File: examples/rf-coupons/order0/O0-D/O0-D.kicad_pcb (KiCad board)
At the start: 4 copper layers, 90.6 x 51.5 mm, 29 parts, among them X20 Anchor, X23 Anchor, X26 Anchor

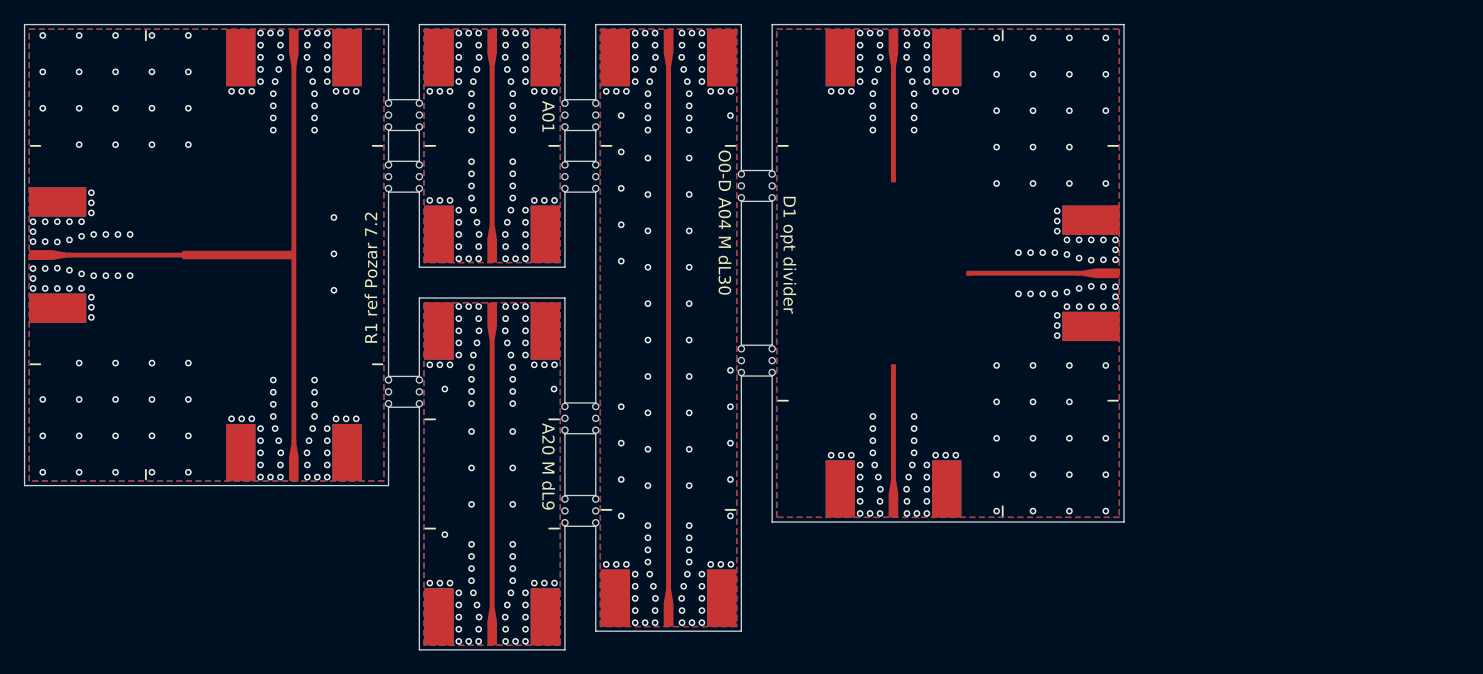
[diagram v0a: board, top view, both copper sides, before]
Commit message: Order 0: D1 re-optimized under the corner-gap DRC (d1-star 7e070ca8), O0-D regenerated, pinned O0-D Gerber hash (#58)
## Summary
- D1 base/robust/star/sched re-run under PR #53's fixed corner-gap DRC
(the committed `d1-star` reproduces two 0.100 mm corner-gap violations
against OSH Park's 0.127 mm rule). `d1-star` ships again — the only
formulation that passes coarse/fine/finer — now with a DRC-clean export;
`d1-base`/`d1-sched` additionally fail *export* DRC under the fixed
checker (not only S-parameters), and `d1-robust` timed out in both of
two submissions (the second with a longer end window and resumed
checkpoints) and is reported inconclusive rather than retried further.
- Registers the winner's 3-substrate validation (M-eq/M-nom/M-eq-em528,
all pass) and a reduced-scope openEMS comparison (new D1 only, 0.05 mm;
R1 reused from part 2 as an unaffected fixed geometry) under
`docs/rf/order0/predictions/D1-d1c/`, compared like for like (openEMS on
nominal FR408HR vs yapnr.rf's M-nom): yapnr.rf puts D1 at the −20 dB
|S11| spec line (−19.70/−20.02/−20.05 dB coarse/fine/finer), openEMS
predicts a 2.9 dB miss (−17.10 dB) — the same disagreement part 2 found
on the old export.
- Palace (the independent second solver) was **not run**: this
workflow's separate $8 GCP cap was reached by the resubmission and the
3-substrate validation before enough ceiling remained; flagged as an
open item in the README rather than silently dropped.
- **Part 5 (added on top of the above): O0-D regenerated** with this
DRC-clean `d1-star` (label `7e070ca8`,
`yapnr.rf.coupons.catalog.D1_WINNER` repointed at
`predictions/D1-d1c/runs/d1-star`): headless KiCad DRC 0 violations / 0
unconnected (zones refilled), `yapnr fab build` 0 errors (2 pre-existing
informational warnings, same pattern as O0-W's build). Panel grows to
118.2 × 50.0 mm, 9.157 sq in, with its own QR label stick A15 to
`predictions/D1-d1c`. Gerber zip sha256 pinned in
`docs/rf/order0/fab/O0-D.sha256`; `sha256-manifest.txt` regene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
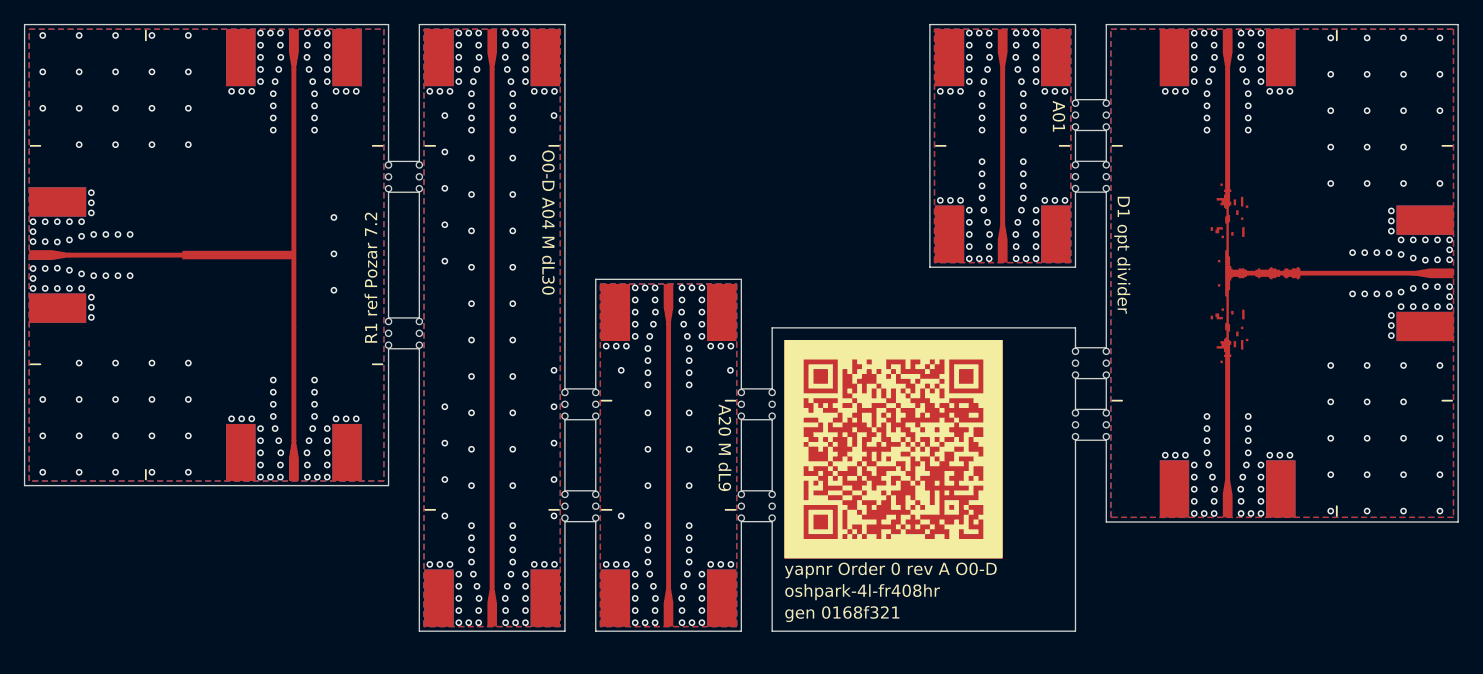
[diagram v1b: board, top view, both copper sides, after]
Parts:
- removed PHD1: Placeholder_D1, Placeholder_D1
- removed X20, X23, X26: Anchor, Anchor
- added UD1: Optimized_D1, Optimized_D1, F.Cu at (119.2, 40.5)
- moved JA01E 42.1 mm to (100.6, 40.0)
- moved JA01W 42.1 mm to (100.6, 20.0)
- moved MO_A01 42.1 mm to (99.4, 22.5)
- moved JD1_1 27.5 mm to (138.2, 40.5)
- moved JD1_2 27.5 mm to (119.2, 61.0)
- moved JD1_3 27.5 mm to (119.2, 20.0)
- moved MO_D1_1 27.5 mm to (125.2, 39.3)
- moved MO_D1_2 27.5 mm to (118.0, 48.0)
- moved MO_D1_3 27.5 mm to (118.0, 22.5)
- moved MO_D1_W 27.5 mm to (112.2, 32.0)
- moved JA20E 14.6 mm to (73.1, 70.0)
- moved JA20W 14.6 mm to (73.1, 41.0)
- moved MO_A20 14.6 mm to (71.9, 43.5)
- moved JA04E 14.5 mm to (58.5, 70.0)
- moved JA04W 14.5 mm to (58.5, 20.0)
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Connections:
- JD1_1 pad 1: RF_D1_1 -> RF_D1
- JD1_2 pad 1: RF_D1_2 -> RF_D1
- JD1_3 pad 1: RF_D1_3 -> RF_D1
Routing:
- net RF_D1: track 0.00 -> 27.9 mm
- net RF_D1_1: track 9.10 -> 0.00 mm
- net RF_D1_3: track 9.09 -> 0.00 mm
- net RF_D1_2: track 9.09 -> 0.00 mm
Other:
- board size 90.6 x 51.5 mm -> 118.2 x 50 mm
- board text added: "7e070ca8"
- board text added: "O0-D A15"
- board text added: "gen 0168f321"
- board text added: "oshpark-4l-fr408hr"
- board text added: "yapnr Order 0 rev A O0-D"
- board text removed: "D1 window 12 x 15"
